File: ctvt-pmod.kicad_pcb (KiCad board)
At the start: 2 copper layers, 33 x 20.3 mm, 0 parts

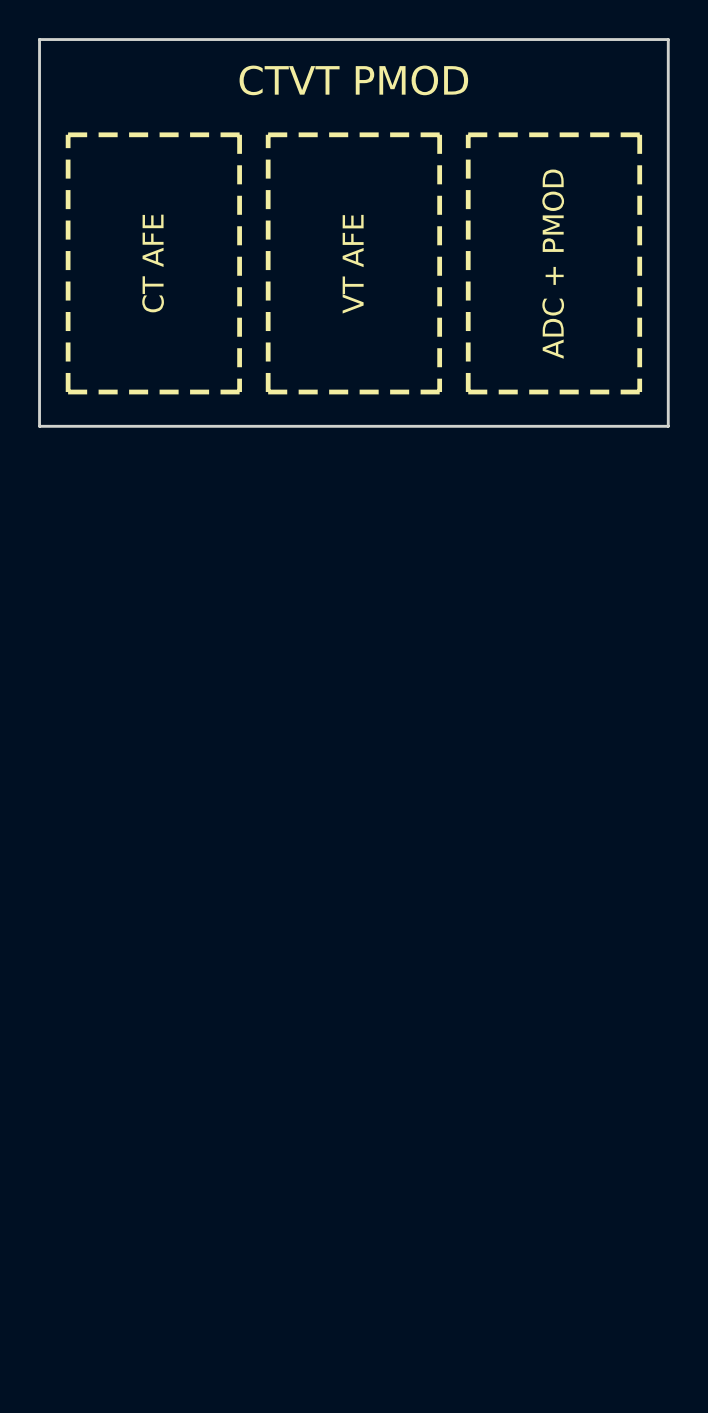
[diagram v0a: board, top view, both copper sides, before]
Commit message: Complete routed CTVT energy monitor PMOD
Implement the ADS131M02 CT/VT analog front end, exact field connectors, chained PMOD interface, reproducible routing and branded fabrication-ready layout. Add architecture, calibration, safety documentation and final board renders.

Co-authored-by: Copilot <223556219+Copilot@users.noreply.github.com>
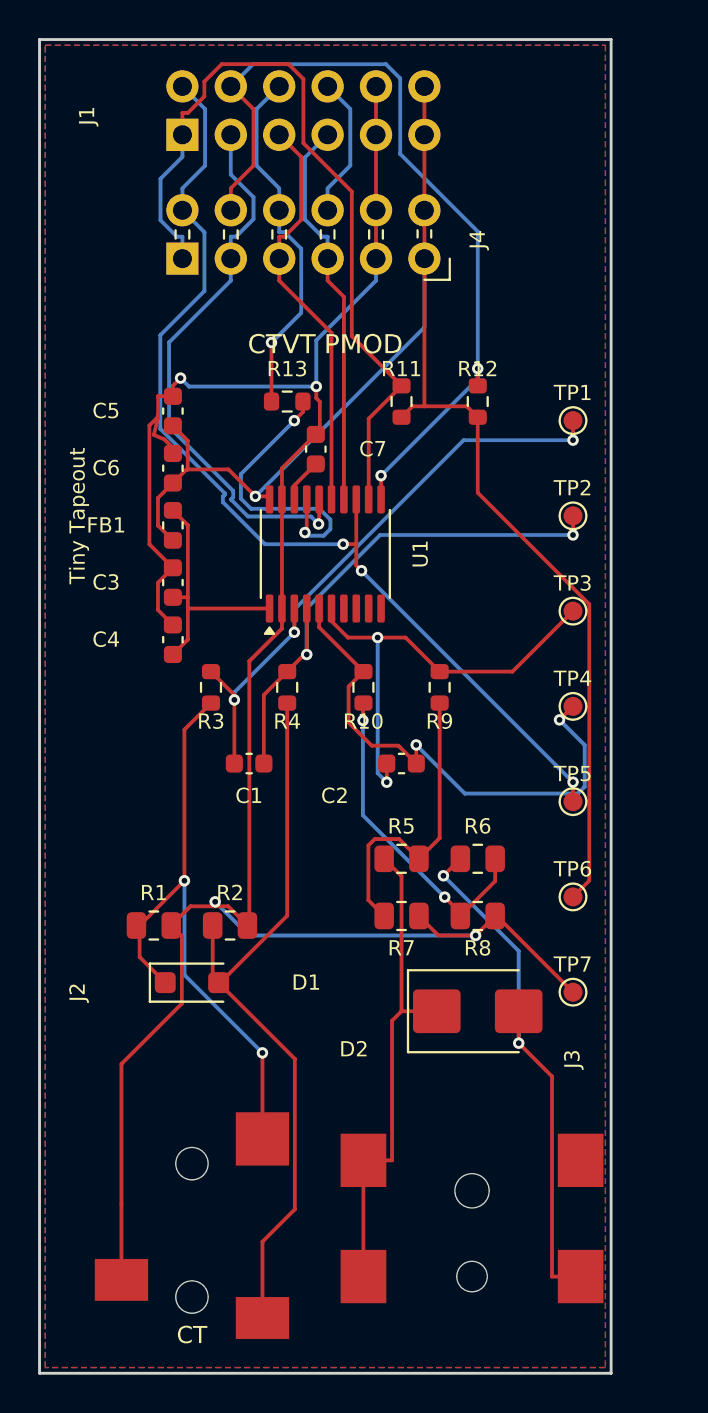
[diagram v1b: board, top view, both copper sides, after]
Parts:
- added C1: 10nF C0G, C_0603_1608Metric, F.Cu at (31.0, 58.0)
- added C2: 10nF C0G, C_0603_1608Metric, F.Cu at (39.0, 58.0)
- added C3: 1uF, C_0603_1608Metric, F.Cu at (27.0, 48.5)
- added C4: 100nF, C_0603_1608Metric, F.Cu at (27.0, 51.5)
- added C5: 1uF, C_0603_1608Metric, F.Cu at (27.0, 39.5)
- added C6: 100nF, C_0603_1608Metric, F.Cu at (27.0, 42.5)
- added C7: 220nF, C_0603_1608Metric, F.Cu at (34.5, 41.5)
- added D1: SMF3.3CA, D_SOD-123F, F.Cu at (28.0, 69.5)
- added D2: SMBJ18CA, D_SMB, F.Cu at (43.0, 71.0)
- added FB1: 600R@100MHz, L_0603_1608Metric, F.Cu at (27.0, 45.5)
- added J1: Tiny Tapeout PMOD, PinHeader_2x06_P2.54mm_Horizontal, F.Cu at (27.5, 25.0)
- added J2: SJ-3523-SMT-TR, Jack_3.5mm_CUI_SJ-3523-SMT_Horizontal, F.Cu at (28.0, 83.5)
- added J3: PJ-002BH-SMT-TR, DC_BARREL_JACK_SMD_2MM, F.Cu at (42.7, 82.7)
- added J4: 613012243121, PinSocket_2x06_P2.54mm_PMODHost1A, F.Cu at (40.2, 31.5)
- added LOGO1: OSHW-LOGO-M, OSHW-LOGO-M, B.Cu at (25.0, 81.0)
- added LOGO2: Whatnick_logo, Whatnick_logo, B.Cu at (35.0, 81.0)
- added R1: 6.49R 0.1%, R_0805_2012Metric, F.Cu at (26.0, 66.5)
- added R10: 1k 0.1%, R_0603_1608Metric, F.Cu at (37.0, 54.0)
- added R11: 10k, R_0603_1608Metric, F.Cu at (39.0, 39.0)
- added R12: 10k, R_0603_1608Metric, F.Cu at (43.0, 39.0)
- added R13: 33R, R_0603_1608Metric, F.Cu at (33.0, 39.0)
- added R2: 6.49R 0.1%, R_0805_2012Metric, F.Cu at (30.0, 66.5)
- added R3: 1k 0.1%, R_0603_1608Metric, F.Cu at (29.0, 54.0)
- added R4: 1k 0.1%, R_0603_1608Metric, F.Cu at (33.0, 54.0)
- added R5: 100k 0.1%, R_0805_2012Metric, F.Cu at (39.0, 63.0)
- added R6: 100k 0.1%, R_0805_2012Metric, F.Cu at (43.0, 63.0)
- added R7: 6.49k 0.1%, R_0805_2012Metric, F.Cu at (39.0, 66.0)
- added R8: 6.49k 0.1%, R_0805_2012Metric, F.Cu at (43.0, 66.0)
- added R9: 1k 0.1%, R_0603_1608Metric, F.Cu at (41.0, 54.0)
- added TP1: AIN0P, TestPoint_Pad_D1.0mm, F.Cu at (48.0, 40.0)
- added TP2: AIN0N, TestPoint_Pad_D1.0mm, F.Cu at (48.0, 45.0)
- added TP3: AIN1P, TestPoint_Pad_D1.0mm, F.Cu at (48.0, 50.0)
- added TP4: AIN1N, TestPoint_Pad_D1.0mm, F.Cu at (48.0, 55.0)
- added TP5: DRDY, TestPoint_Pad_D1.0mm, F.Cu at (48.0, 60.0)
- added TP6: +3V3, TestPoint_Pad_D1.0mm, F.Cu at (48.0, 65.0)
- added TP7: GND, TestPoint_Pad_D1.0mm, F.Cu at (48.0, 70.0)
- added U1: ADS131M02IPWR, TSSOP-20_4.4x6.5mm_P0.65mm, F.Cu at (35.0, 47.0)
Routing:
- net GND: track 0.00 -> 122.2 mm, vias 0 -> 4
- net +3V3: track 0.00 -> 77.7 mm, vias 0 -> 1
- net DRDY: track 0.00 -> 54.2 mm, vias 0 -> 3
- net RESET: track 0.00 -> 44.0 mm, vias 0 -> 2
- net CS: track 0.00 -> 41.9 mm
- net CT_N: track 0.00 -> 39.3 mm
- net CT_P: track 0.00 -> 32.2 mm, vias 0 -> 2
- net AIN0P: track 0.00 -> 32.0 mm, vias 0 -> 3
- net MOSI: track 0.00 -> 29.5 mm, vias 0 -> 1
- net AIN0N: track 0.00 -> 28.1 mm, vias 0 -> 2
- net VT_N: track 0.00 -> 27.8 mm, vias 0 -> 2
- net AIN1N: track 0.00 -> 27.8 mm, vias 0 -> 2
- net VT_P: track 0.00 -> 25.9 mm
- net AIN1P: track 0.00 -> 24.5 mm, vias 0 -> 2
- net MISO: track 0.00 -> 21.4 mm
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- added copper zone on B.Cu, net GND
- added copper zone on F.Cu, net GND
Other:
- board size 33 x 20.3 mm -> 30 x 70 mm
- board text added: "AC-AC ONLY"
- board text added: "CT"
- board text added: "NO DIRECT MAINS"
- board text added: "REV 1.0 | CERN-OHL-S-2.0+"
- board text added: "Tiny Tapeout"
- board text added: "by Tisham Dhar https://whatnick.com Rev 1.0 20/09/2026"
- board text removed: "ADC + PMOD"
- board text removed: "CT AFE"
- board text removed: "PLACEHOLDER - NOT FOR MEASUREMENT"
- board text removed: "VT AFE"

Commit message: Capture final silkscreen hierarchy
Preserve the manual 0.8 mm/0.2 mm silkscreen normalization, aligned references, front-side Whatnick and Tiny Tapeout identity, and rear safety/legal markings in the generators. Refresh README renders with the complete board and connector overhangs visible.

Co-authored-by: Copilot <223556219+Copilot@users.noreply.github.com>
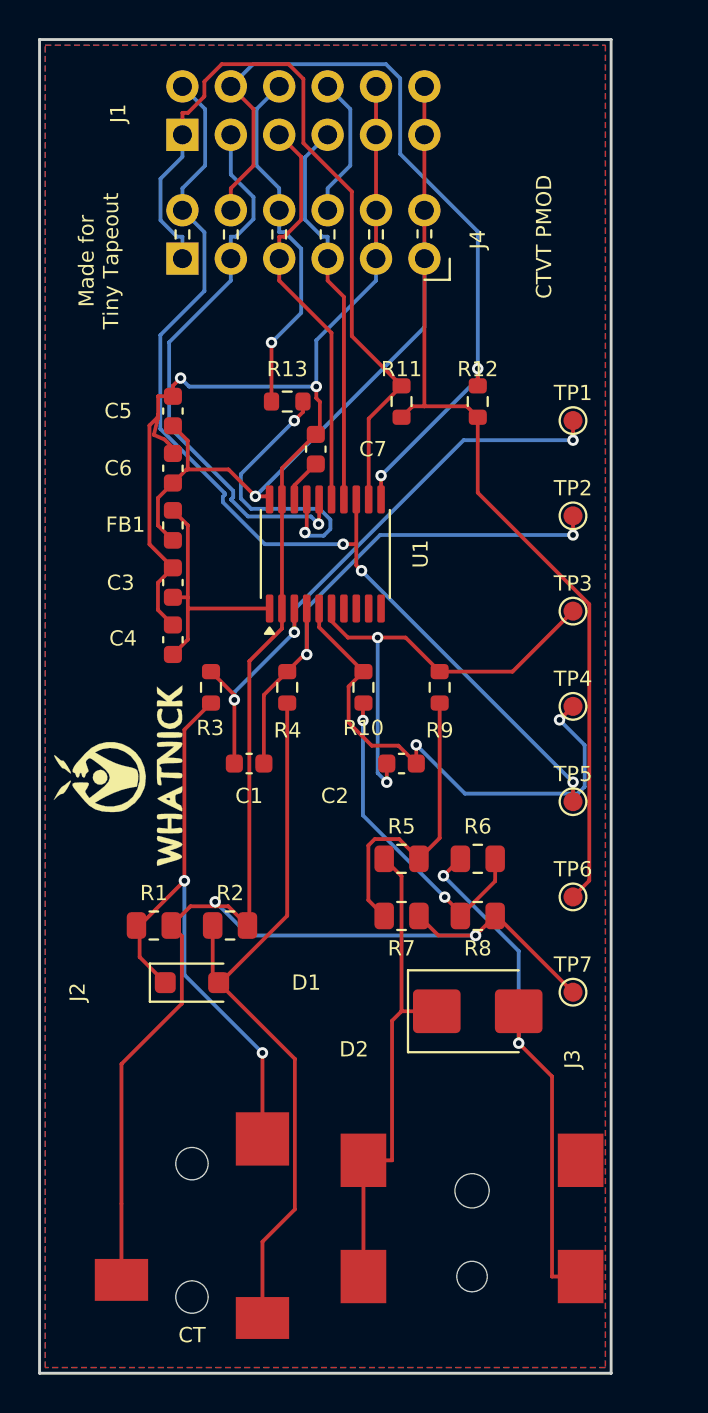
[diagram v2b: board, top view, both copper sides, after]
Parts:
- LOGO2: moved to F.Cu
- moved LOGO2 24.8 mm to (24.1, 58.7), turned to 90 degrees
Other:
- board text added: "Made for Tiny Tapeout"
- board text removed: "Tiny Tapeout"

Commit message: Round board corners and add mounting holes
Apply 3 mm radii to the 30 x 70 mm outline and add two accessible M2 NPTH mounting holes at the PMOD end without disturbing the connector edge. Preserve the mechanical update in the board generator and a standalone post-route script, move the J1 reference clear of the new hole, and refresh all README renders.

Co-authored-by: Copilot <223556219+Copilot@users.noreply.github.com>
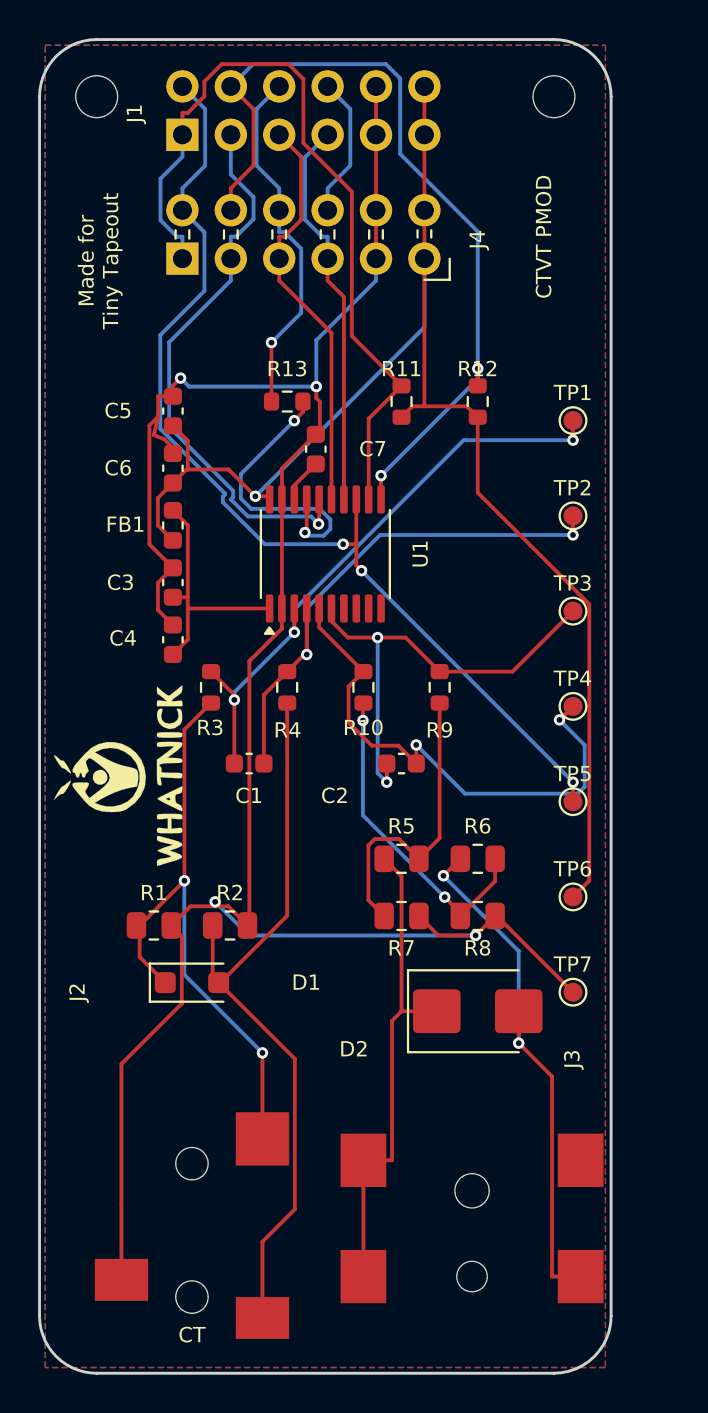
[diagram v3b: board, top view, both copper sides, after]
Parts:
- added H1: M2 mounting hole, MountingHole_2.2mm_M2, F.Cu at (23.0, 23.0)
- added H2: M2 mounting hole, MountingHole_2.2mm_M2, F.Cu at (47.0, 23.0)
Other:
- outline, holes or cut-outs redrawn

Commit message: Widen all routed traces
Reroute the unchanged CTVT PMOD placement at a uniform 0.25 mm trace width with 0.20 mm clearance. Persist the wider default in KiCad settings and generators, replace the Freerouting session, reduce the route from 29 to 11 vias, and refresh all board renders.

Co-authored-by: Copilot <223556219+Copilot@users.noreply.github.com>
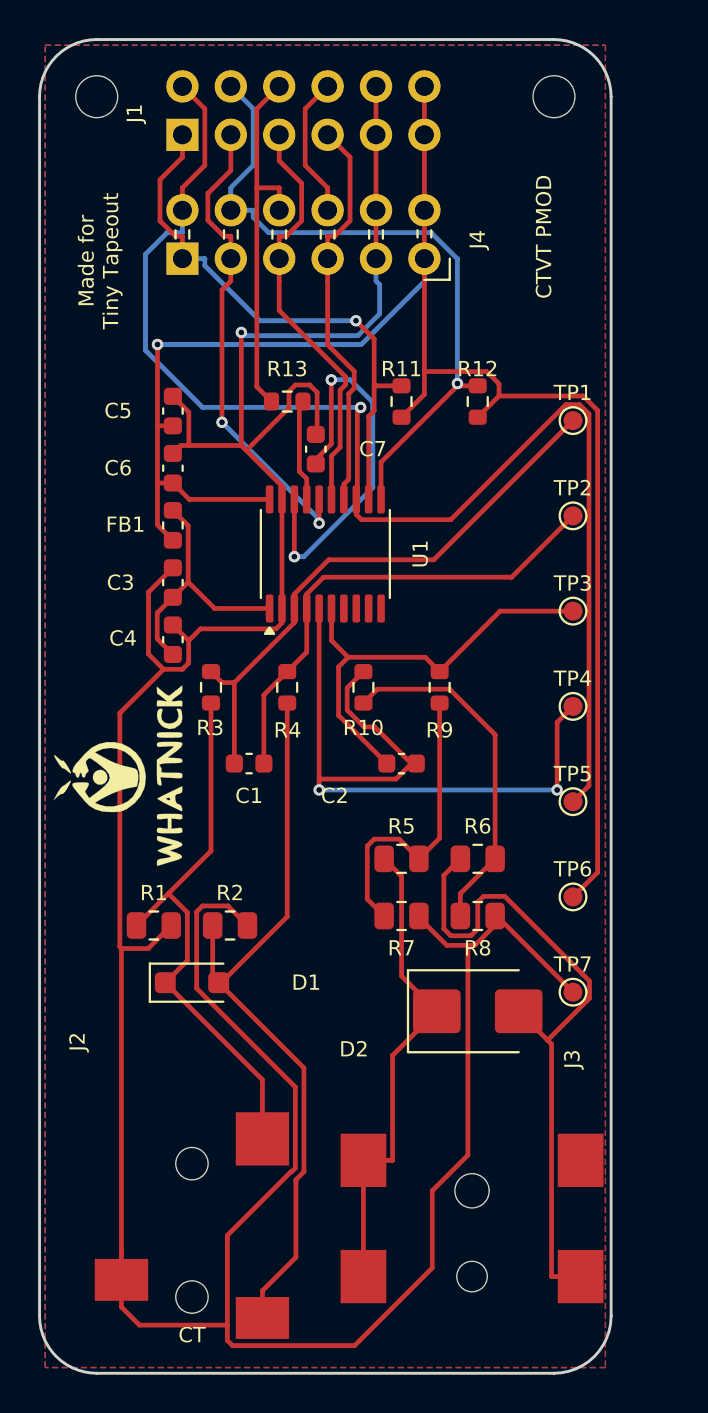
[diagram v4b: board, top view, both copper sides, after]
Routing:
- net GND: track 122.2 -> 180.4 mm, vias 4 -> 1
- net CAP: track 2.33 -> 20.5 mm, vias 0 -> 2
- net DRDY: track 54.2 -> 70.1 mm, vias 3 -> 1
- net +3V3: track 77.7 -> 90.1 mm
- net CS: track 41.9 -> 29.7 mm, vias 0 -> 1
- net AIN1N: track 27.8 -> 39.1 mm
- net CLKIN: track 15.4 -> 5.38 mm, vias 2 -> 0
- net RESET: track 44.0 -> 36.0 mm, vias 2 -> 1
- net VT_N: track 27.8 -> 35.5 mm, vias 2 -> 0
- net MOSI: track 29.5 -> 25.2 mm, vias 1 -> 2
- net CT_P: track 32.2 -> 29.2 mm, vias 2 -> 0
- net AIN0N: track 28.1 -> 25.5 mm, vias 2 -> 0
- net AIN0P: track 32.0 -> 30.1 mm, vias 3 -> 0
- net VT_DIV_N: track 17.1 -> 18.5 mm, vias 2 -> 0
- net AIN1P: track 24.5 -> 23.2 mm, vias 2 -> 0
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
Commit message: Center both PMOD connectors
Co-authored-by: Copilot <223556219+Copilot@users.noreply.github.com>
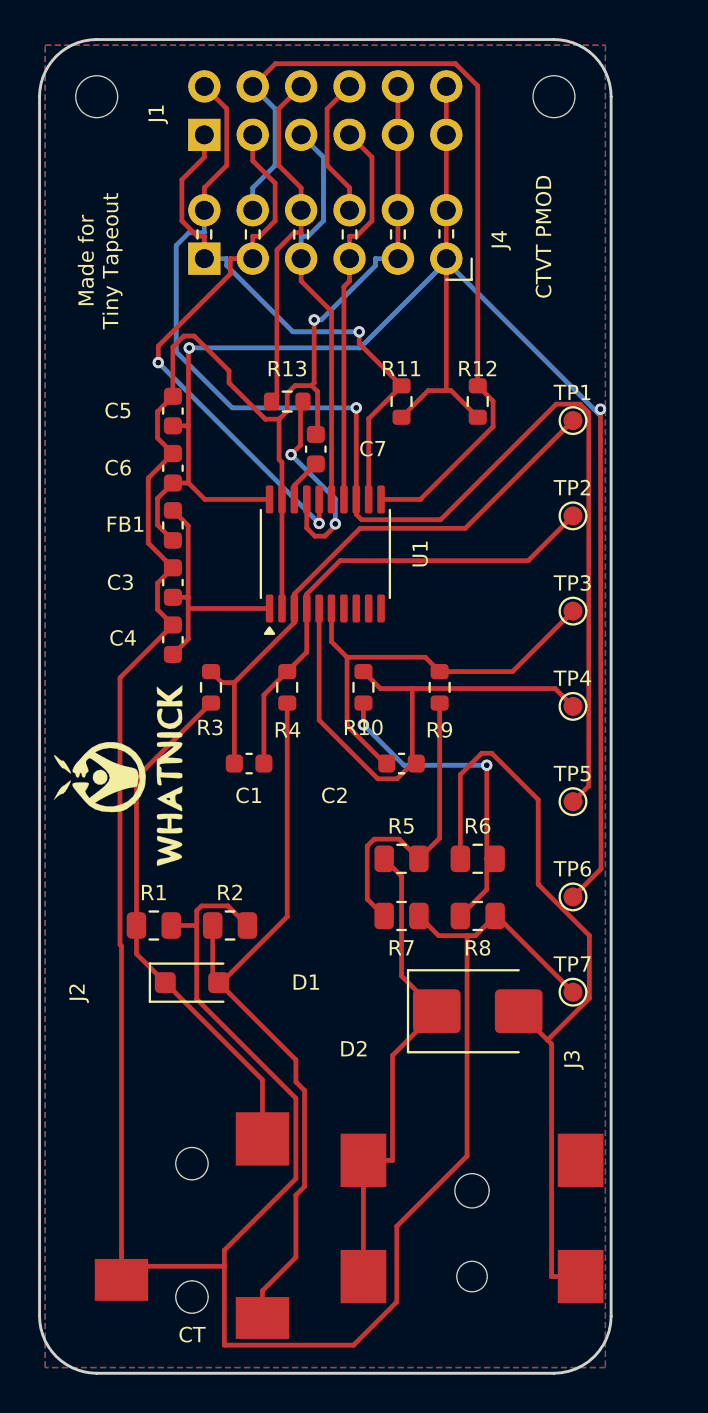
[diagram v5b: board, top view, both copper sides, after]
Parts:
- moved J1 1.15 mm to (28.6, 25.0)
- moved J4 1.15 mm to (41.4, 31.5)
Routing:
- net CAP: track 20.5 -> 2.33 mm, vias 2 -> 0
- net AIN1N: track 39.1 -> 28.3 mm, vias 2 -> 0
- net RESET: track 36.0 -> 45.9 mm, vias 1 -> 0
- net GND: track 180.4 -> 172.5 mm
- net CLKIN: track 5.38 -> 11.1 mm, vias 0 -> 2
- net VT_N: track 35.5 -> 40.8 mm
- net MOSI: track 25.2 -> 29.1 mm
- net DRDY: track 70.1 -> 68.0 mm
- net CT_P: track 29.2 -> 27.2 mm
- net CS: track 29.7 -> 28.1 mm
- net +3V3: track 90.1 -> 91.6 mm, vias 1 -> 2
- net CLK_HOST: track 19.7 -> 18.4 mm
- net MISO: track 22.1 -> 21.0 mm
- net VT_DIV_N: track 18.5 -> 17.4 mm, vias 0 -> 2
- net SCLK: track 21.1 -> 20.4 mm

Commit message: Prepare Elecrow PCBA manufacturing package
Correct J4 to the vertical Wurth 61301221821 socket, add deterministic KiCad 10 manufacturing exports, and include verified Gerber, BOM, position, and combined Elecrow upload archives.

Co-authored-by: Copilot <223556219+Copilot@users.noreply.github.com>
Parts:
- J4: value 613012243121 -> 61301221821
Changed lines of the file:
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@@
 			)
 		)
-		(property "Value" "613012243121"
+		(property "Value" "61301221821"
 			(at -5.65 15.47 270)
 			(layer "F.Fab")
